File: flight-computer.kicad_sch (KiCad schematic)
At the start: 21 parts

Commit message: Added power circuitry and status LEDs. Went for an LDO with very low dropout voltage to reduce potential noise from a switching reg.
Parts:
- removed J?: ARM, minifit-jr:MOLEX_1726480102, symbol 1726480102:Minifit-JR-2pos
- removed R?: 1k, symbol Device:R
- added BZ?: Active Buzzer, symbol Device:Buzzer
- added C? (x10): 100n, symbol Device:C
- added C?: 1u, symbol Device:C
- added D?: GREEN LED, symbol Device:LED
- added D?: RED LED, symbol Device:LED
- added R?: 10k, symbol Device:R
- added R? (x3): 1k, symbol Device:R
- added SW?: SW_Push, symbol Switch:SW_Push
- J?: value MEM2067-02-180-00-A -> MicroSD Slot
- Y?: footprint (none) -> Crystal:Crystal_SMD_3225-4Pin_3.2x2.5mm
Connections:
- net QSPI_SS is gone; now on net BOOT: U?.1 (~{CS}), U?.56 (QSPI_SS)
- net +3V3: now also C?.1, C?.1, C?.1, C?.1, C?.1, C?.1, C?.1, C?.1, C?.1, R?.1
- net BOOT: now also R?.2; no longer SW?.2
- net GND: now also U?.19 (TESTEN), U?.57 (GND), BZ?.2 (-), C?.2, C?.2, C?.2, C?.2, C?.2, C?.2, C?.2, C?.2, C?.2, C?.2, C?.2, R?.2, R?.2, SW?.1
- net +1V1: now reaches U?.23 (DVDD), U?.45 (VREG_VOUT), U?.50 (DVDD)
- net +1V1: now also C?.1, C?.1
- net RUN: now reaches U?.26 (RUN)
- net RUN: now also R?.2, SW?.2
- net BUZZ: now reaches U?.35 (GPIO23)
- net BUZZ: now also BZ?.1 (+)
- net STARTUP: now reaches U?.36 (GPIO24)
- net STARTUP: now also D?.2 (A)
- net PANIC: now reaches U?.37 (GPIO25)
- net PANIC: now also D?.2 (A)
- new net: D?.1 (K), R?.1 (x2)
- new net: R?.1, SW?.2
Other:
- added sheet Power (power.kicad_sch)
- note added: "ADC_AVDD"
- note added: "Auditory arming indicator"
- note added: "DVDD"
- note added: "Decoupling capacitors"
- note added: "IOVDD"
- note added: "Kernel Panic"
- note added: "Kernel startup"
- note added: "RESET"
- note added: "Recommended: ABM8-272-T3"
- note added: "USB_VDD"
- note added: "VREG_VIN"
- note removed: "Arming switch terminal"
- note removed: "Shorting the two terminals of this connector will connect the regulator output to the power supply of the board. This allows any arming switch mechanism to be used."
- moved on the sheet: C?, J?, R?, SW?, U?, Y?

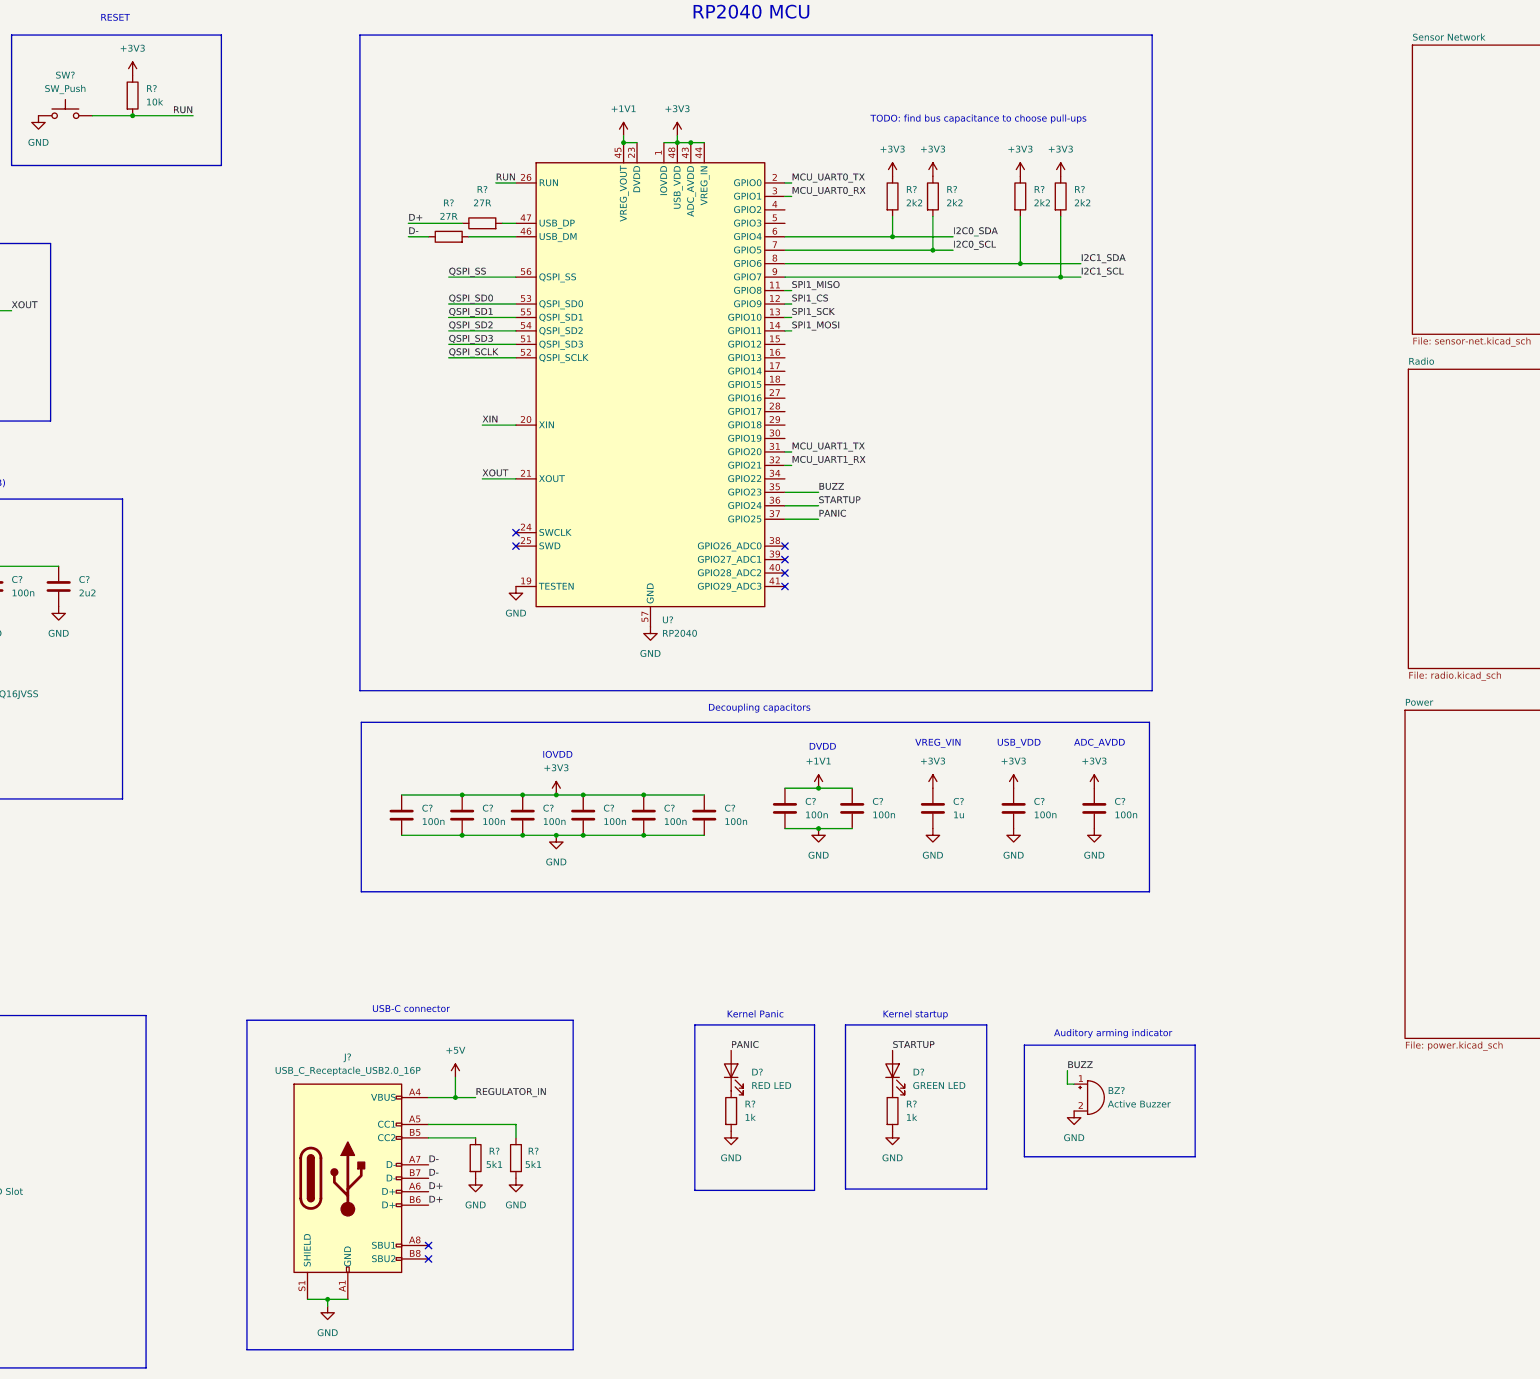
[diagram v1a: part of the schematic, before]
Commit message: Added decoupling caps to RN2483 and fixed antenna connection. Also settled on easy GPS.
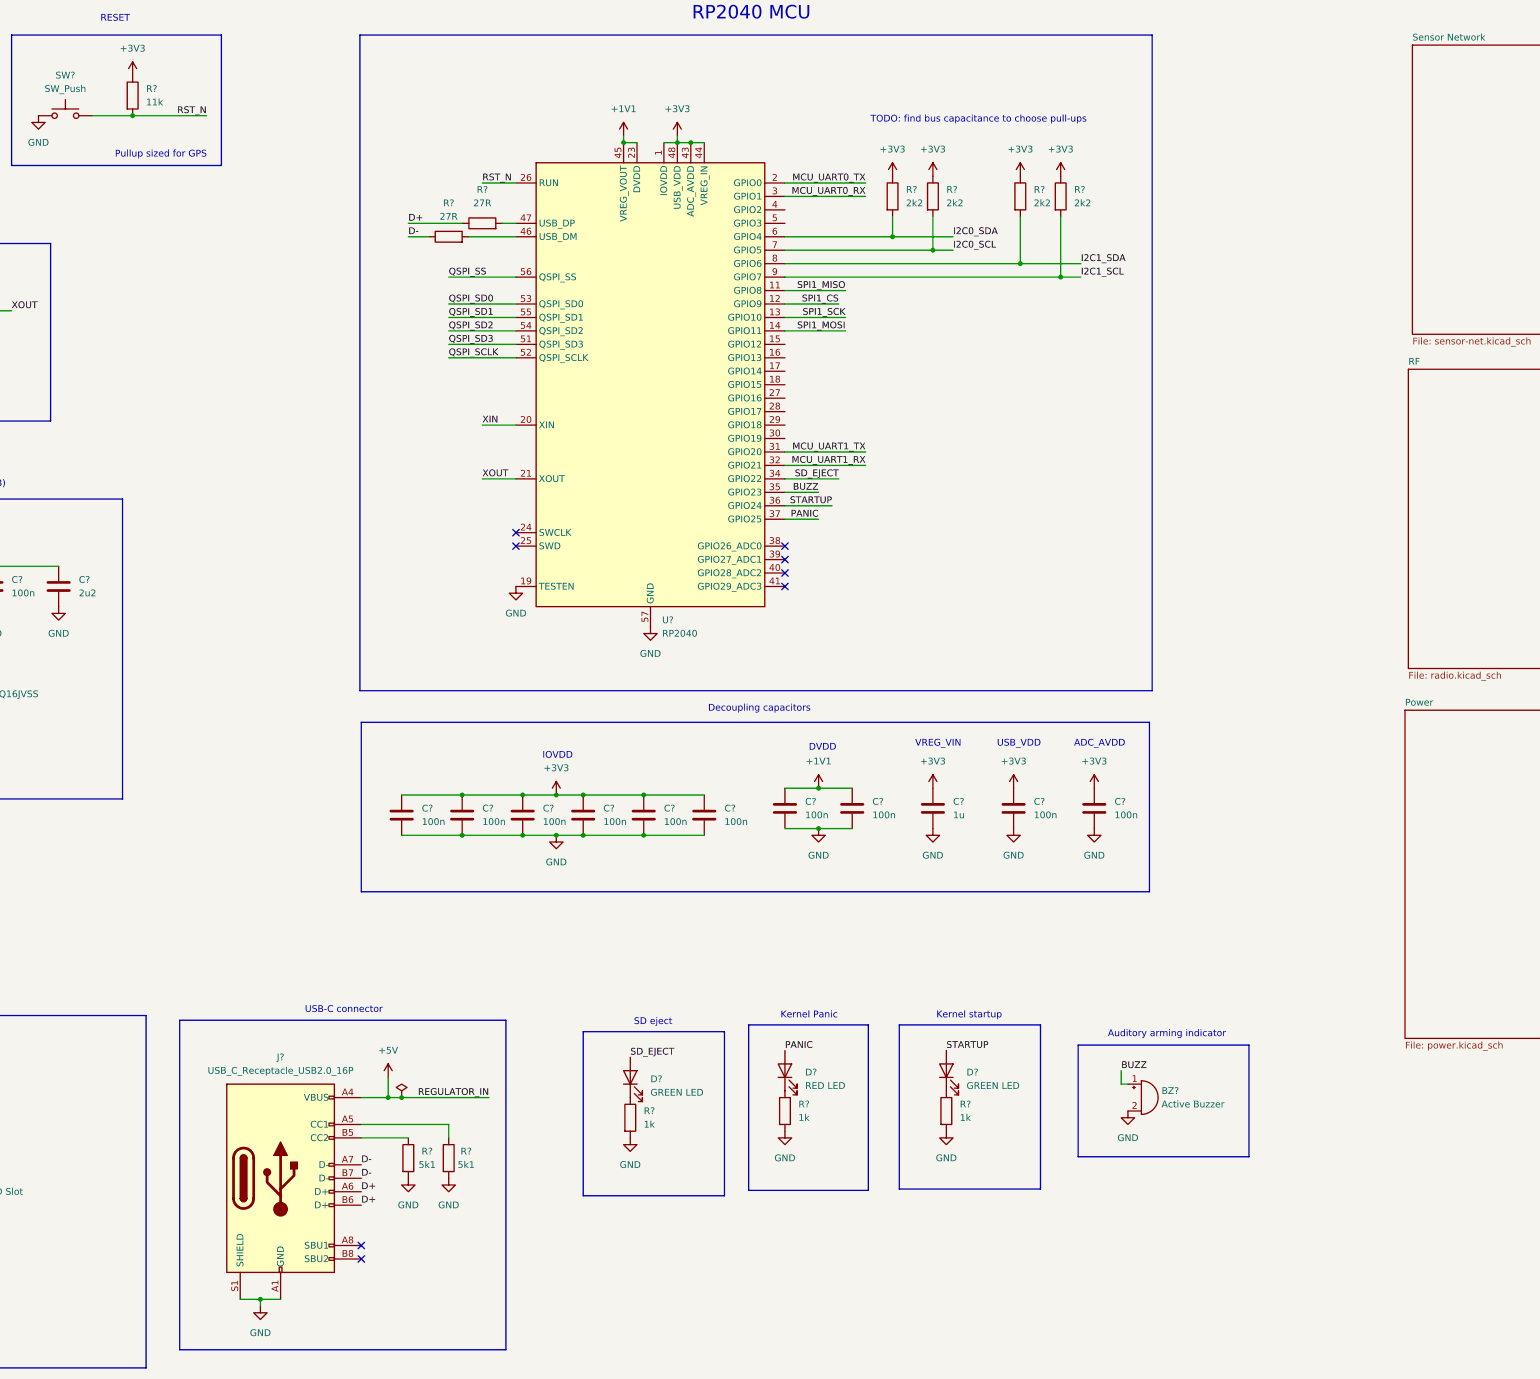
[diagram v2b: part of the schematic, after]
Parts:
- added D?: GREEN LED, symbol Device:LED
- added R?: 1k, symbol Device:R
- R?: value 10k -> 11k
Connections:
- net GND: now also R?.2
- net SD_EJECT: now reaches U?.34 (GPIO22)
- net SD_EJECT: now also D?.2 (A)
- net RUN renamed RST_N
- new net: D?.1 (K), R?.1
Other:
- sheet Radio renamed RF
- note added: "Pullup sized for GPS"
- note added: "SD eject"
- moved on the sheet: BZ?, D?, J?, R?

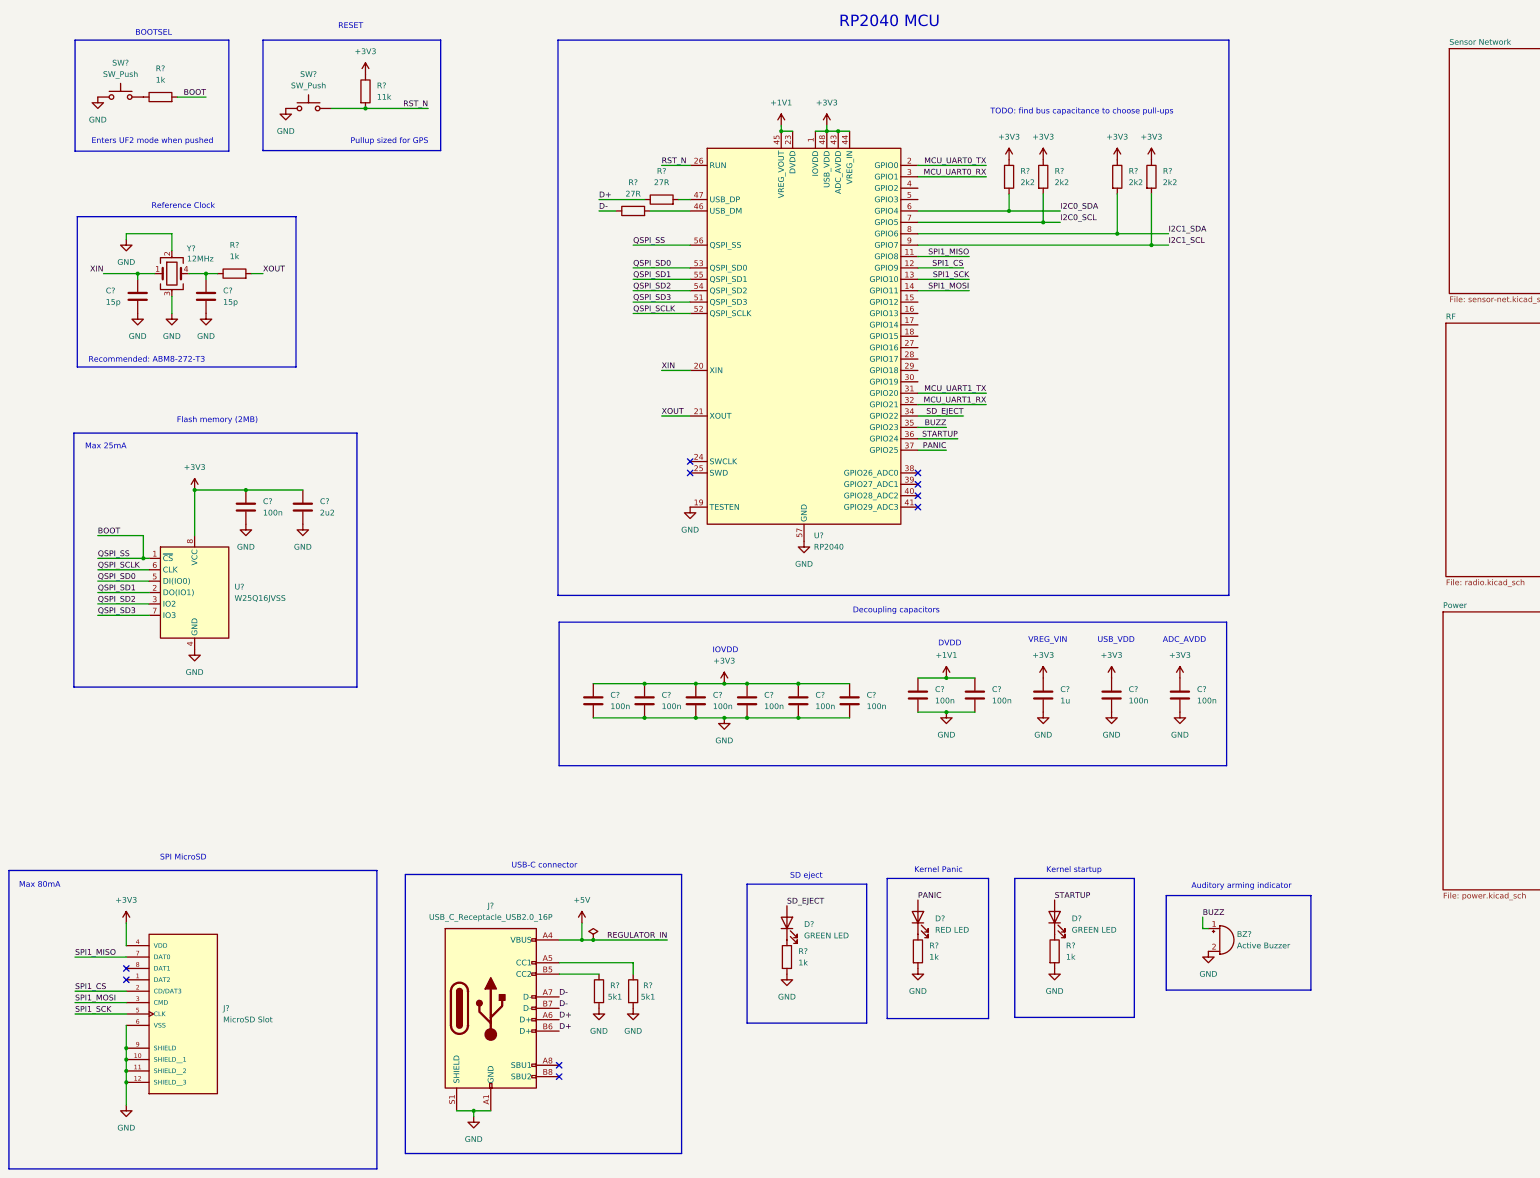
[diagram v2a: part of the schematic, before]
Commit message: Updated power supply to use buck regulator and power input MUX. Also computed current draw of the board to size power regulator.
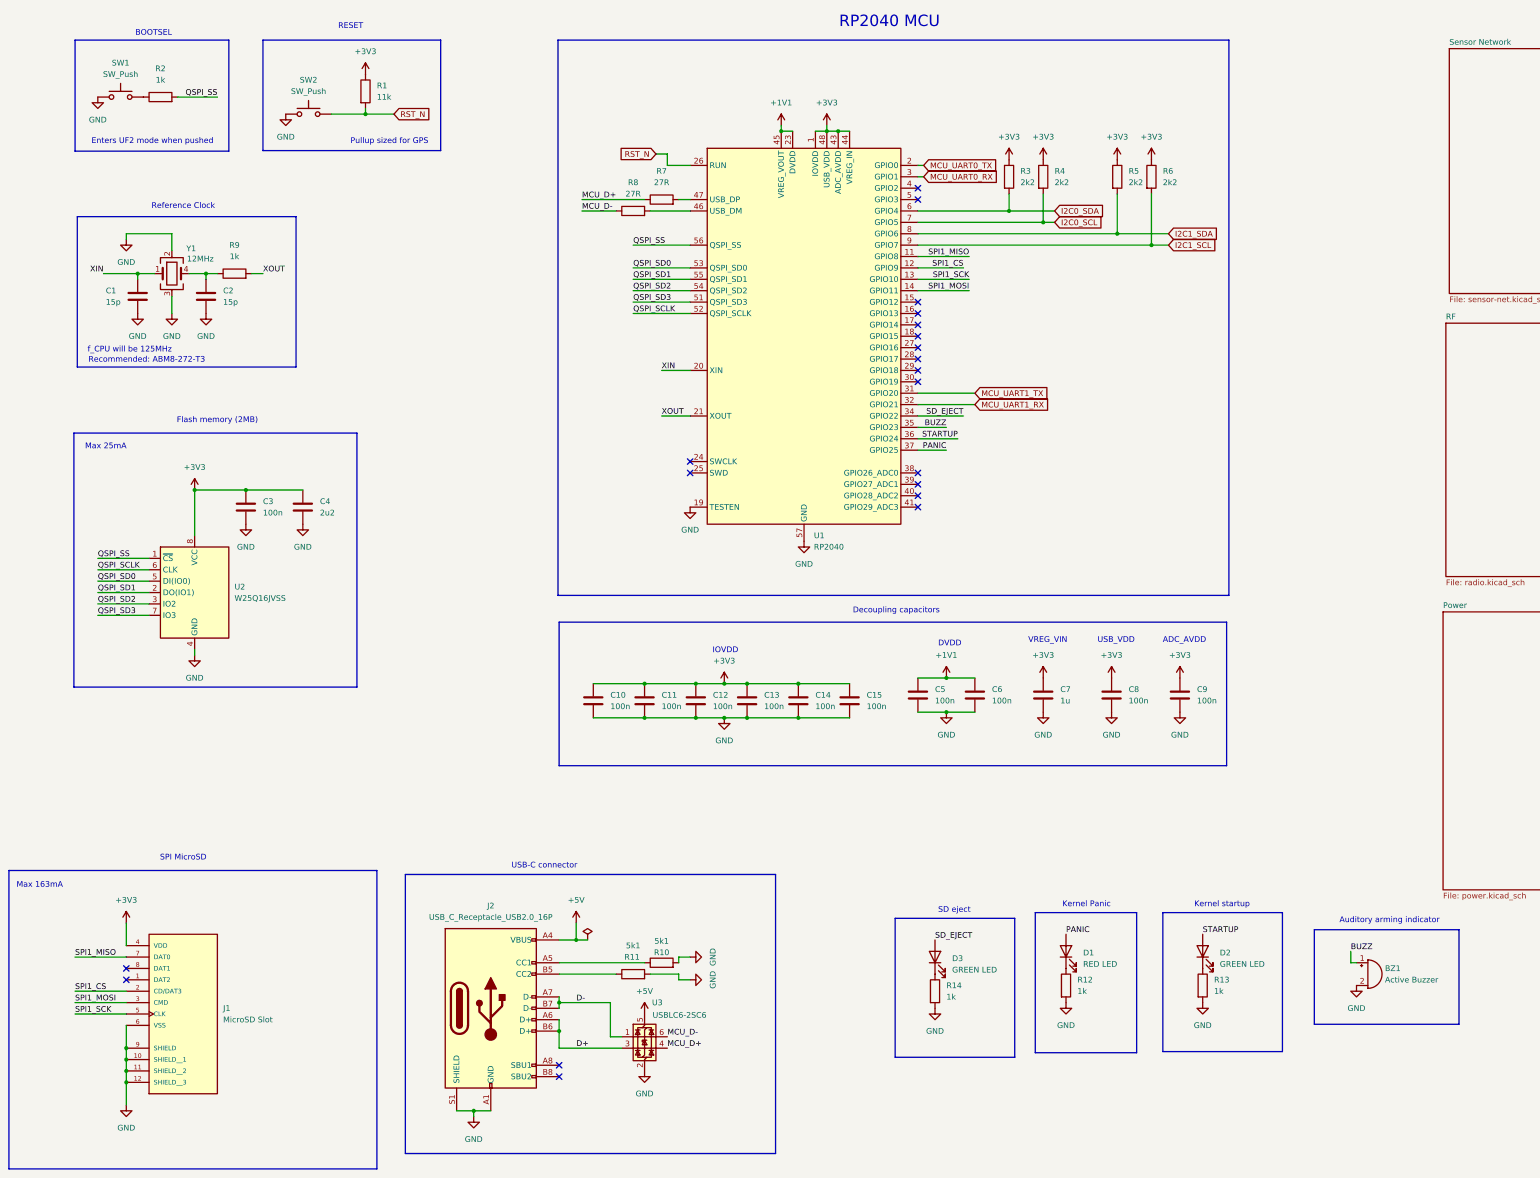
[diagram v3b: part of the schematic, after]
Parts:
- added U3: USBLC6-2SC6, Package_TO_SOT_SMD:SOT-23-6, symbol Power_Protection:USBLC6-2SC6
- gave numbers to parts that had none: 40
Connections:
- net +5V: now also U3.5 (VBUS)
- net D+: now also U3.3 (I/O2); no longer R7.1
- net D-: now also U3.1 (I/O1); no longer R8.1
- net GND: now also U3.2 (GND)
- net BOOT renamed QSPI_SS
- new net MCU_D+: R7.1, U3.4 (I/O2)
- new net MCU_D-: R8.1, U3.6 (I/O1)
- no-connect marks 10 -> 20
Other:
- note added: "Max 163mA"
- note added: "f_CPU will be 125MHz"
- note removed: "Max 80mA"
- note removed: "TODO: find bus capacitance to choose pull-ups"
- moved on the sheet: BZ1, D1, D2, D3, R10, R11, R12, R13, R14, SW2

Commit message: Added footprints for all components
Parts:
- added R15: 150R, Resistor_SMD:R_0201_0603Metric, symbol Device:R
- BZ1: footprint (none) -> buzzer:XDCR_AI-1223-TWT-3V-2-R
- C1, C2: footprint (none) -> Capacitor_SMD:C_0402_1005Metric
- C10, C11, C12, C13, C14, C15, C3, C5, C6, C8, C9: footprint (none) -> Capacitor_SMD:C_0201_0603Metric
- C4, C7: footprint (none) -> Capacitor_SMD:C_0603_1608Metric
- D1, D2, D3: footprint (none) -> LED_SMD:LED_0805_2012Metric
- J2: footprint (none) -> Connector_USB:USB_C_Receptacle_GCT_USB4105-xx-A_16P_TopMnt_Horizontal
- R1, R10, R11, R12, R13, R14, R2, R3, R4, R5, R6, R9: footprint (none) -> Resistor_SMD:R_0201_0603Metric
- R7, R8: footprint (none) -> Resistor_SMD:R_0603_1608Metric
- SW1, SW2: footprint (none) -> Button_Switch_THT:SW_PUSH_6mm_H5mm
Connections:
- net GND: now also R15.2; no longer BZ1.2 (-)
- new net: BZ1.2 (-), R15.1
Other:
- moved on the sheet: BZ1
